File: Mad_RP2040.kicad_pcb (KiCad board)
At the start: 2 copper layers, 38 x 32.1 mm, 65 parts, among them J1 USB_C_Receptacle, J2 Conn_ARM_SWD_TagConnect_TC203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, Q1 2N7002VC-7, SW1 SW_SPST, SW2 SW_SPST, SW3 TL3780AF240QG, U0 PCB, U1 ECMF02-2AMX6, U3 NCP1117-3.3_SOT223, U4 GD25Q127CWIGR, U5 RP2040, X1 ECS-2520MVLC-120-CN

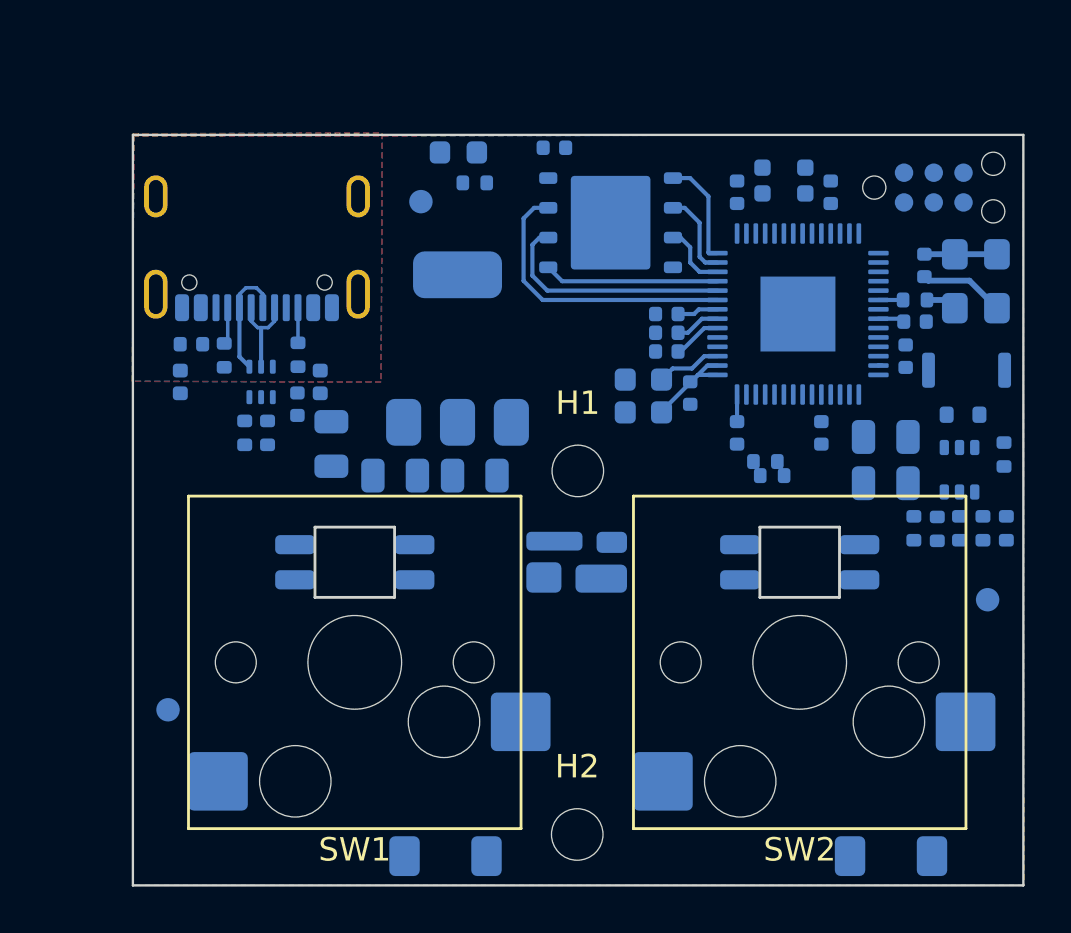
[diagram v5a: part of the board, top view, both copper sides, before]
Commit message: BOM update, add lcsc pn to  componenets.
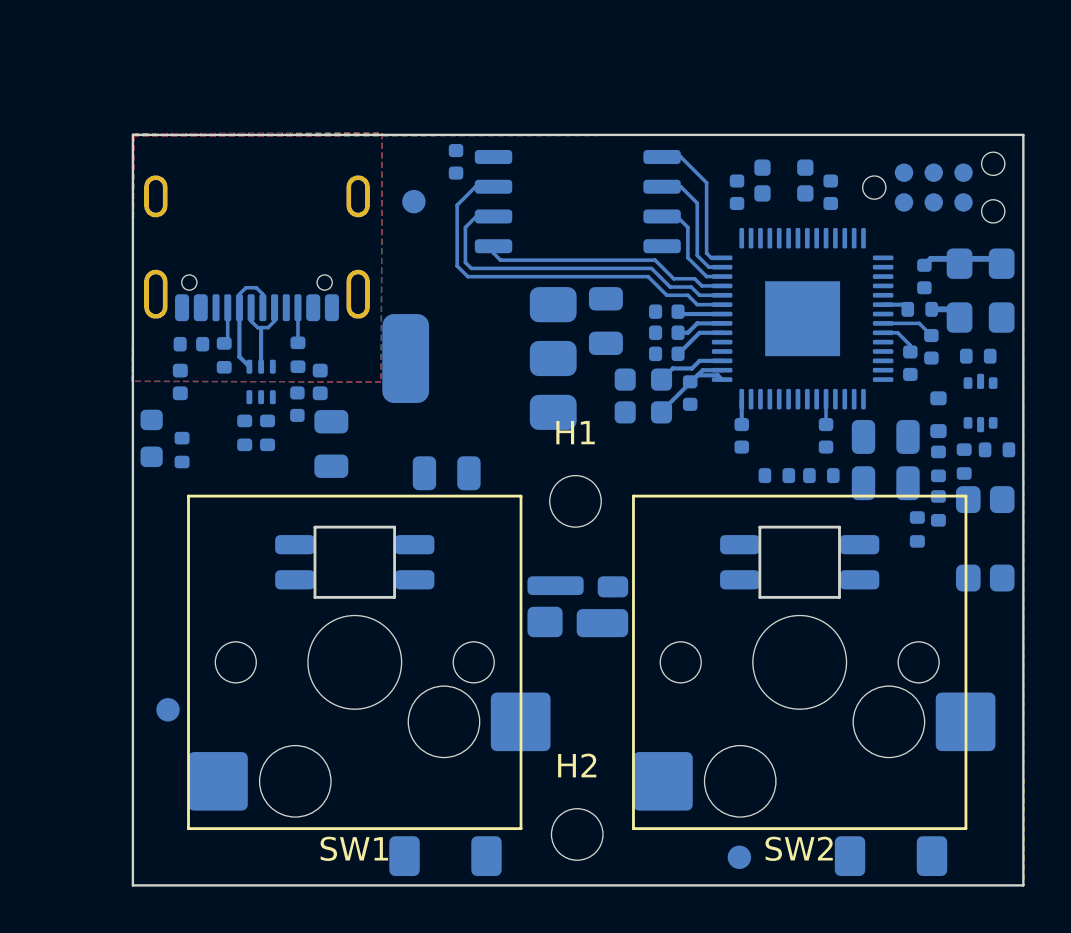
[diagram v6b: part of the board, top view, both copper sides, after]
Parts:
- D5: value WS2812B-2020 -> WS2812C-2020-V1
- D8: value SK6812MINI-012 -> SK6812MINI
- Q1: value 2N7002VC-7 -> 2N7002PV,115; footprint Package_TO_SOT_SMD:SOT-363_SC-70-6 -> Package_TO_SOT_SMD:SOT-666
- SW3: value TL3780AF240QG -> EVPAA202K; footprint Mad_Footprints:SW_TL3780AF240QG -> Mad_Footprints:EVP-AA202K
- U4: value GD25Q127CWIGR -> W25Q128JVSIQ; footprint Mad_Footprints:GD25LQ128DYIGR -> Package_SO:SOIC-8_5.23x5.23mm_P1.27mm
- moved D6 17.9 mm to (122.8, 84.7), turned to -90 degrees
- moved R5 16.9 mm to (124.0, 85.2), turned to 90 degrees
- moved FID1 15.3 mm to (147.8, 102.6)
- moved C5 8.66 mm to (142.2, 79.7), turned to 90 degrees
- moved R7 7.85 mm to (158.1, 81.2), turned to 180 degrees
- moved SW3 7.24 mm to (158.3, 89.0), turned to 90 degrees
- moved C6 4.24 mm to (135.8, 72.9), turned to 90 degrees
- moved R11 3.02 mm to (156.3, 87.7), turned to -90 degrees
- moved Q1 2.99 mm to (158.2, 83.2), turned to 90 degrees
- moved R12 2.96 mm to (157.4, 85.7)
- moved R8 2.89 mm to (156.3, 85.8), turned to 90 degrees
- moved R4 2.46 mm to (151.3, 86.3), turned to 0 degrees
- moved C4 2.20 mm to (135.3, 86.2)
- moved D8 1.90 mm to (140.9, 91.9)
- moved U4 1.66 mm to (140.9, 74.6)
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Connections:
- Q1 pad 3: GND -> Net-(Q1B-D)
- Q1 pad 4: Net-(Q1B-S) -> GND
- R12 pad 1: Net-(Q1B-S) -> Net-(Q1B-D)
- SW3 pad 1: Net-(D7-A) -> /RP2040/3V3
- SW3 pad 2: /RP2040/3V3 -> Net-(D7-A)
- TP3 pad 1: Net-(Q1B-S) -> Net-(Q1B-D)
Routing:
- net /RP2040/RP2040/QSPI_SCLK: track 10.3 -> 14.4 mm
- net /RP2040/RP2040/QSPI_SD3: track 12.5 -> 16.5 mm
- net GND: track 3.66 -> 0.00 mm
- net /RP2040/3V3: track 13.5 -> 16.7 mm
- net /RP2040/RP2040/QSPI_SD0: track 7.47 -> 10.6 mm
- net /RP2040/RP2040/1V1: track 4.57 -> 6.51 mm
- net /RP2040/RP2040/QSPI_SD1: track 3.72 -> 5.30 mm
- net /RP2040/RP2040/QSPI_SD2: track 2.89 -> 4.39 mm
- net /RP2040/RP2040/QSPI_~{CS}: track 4.63 -> 6.11 mm

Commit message: BOM consolidation
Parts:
- removed FID2: Fiducial, Fiducial:Fiducial_1mm_Mask2mm
- removed TP1: Reset, TestPoint:TestPoint_Pad_D1.0mm
- removed TP2: Delay, TestPoint:TestPoint_Pad_D1.0mm
- removed TP3: Boot, TestPoint:TestPoint_Pad_D1.0mm
- added D9: B5817WS, Diode_SMD:D_SOD-323, B.Cu at (131.3, 85.1)
- added F1: 500mA, Fuse:Fuse_0402_1005Metric, B.Cu at (131.3, 83.0)
- added R15: 51K, Resistor_SMD:R_0402_1005Metric, B.Cu at (154.4, 88.6)
- FB1: value BLM15PX330SN1D -> 33 Ohms Ferrite
- R9: value 100K -> 51K
- U3: value NCP1117-3.3_SOT223 -> NCP1117-3.3
- U4: footprint Package_SO:SOIC-8_5.23x5.23mm_P1.27mm -> Mad_Footprints:SOIC-8_5.23x5.23mm_P1.27mm
- moved D6 16.3 mm to (134.2, 73.2)
- moved R5 13.9 mm to (134.2, 75.7), turned to -90 degrees
- moved C2 4.22 mm to (130.4, 87.2), turned to 180 degrees
- moved C3 0.98 mm to (129.4, 85.0)
- moved R13 0.36 mm to (127.0, 84.2)
- moved R14 0.31 mm to (127.8, 84.2)
- moved U1 0.20 mm to (127.4, 82.1)
- turned R9 to -90 degrees
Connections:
- net Net-(U5-D+) renamed /RP2040/RP2040/USB_D+
- net Net-(U5-D-) renamed /RP2040/RP2040/USB_D-
- FB1 pad 2: +5V -> Net-(F1-Pad2)
- R9 pad 1: GND -> Net-(Q1B-G)
- R9 pad 2: Net-(Q1B-G) -> Net-(R15-Pad1)
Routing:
- net GND: track 0.00 -> 11.1 mm
- net /RP2040/RP2040/USB_D-: track 0.00 -> 0.61 mm, vias 0 -> 1
- net /RP2040/RP2040/USB_D+: track 0.00 -> 0.56 mm, vias 0 -> 1
